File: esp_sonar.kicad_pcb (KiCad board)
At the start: 2 copper layers, 5 parts, among them Q1 2N4401

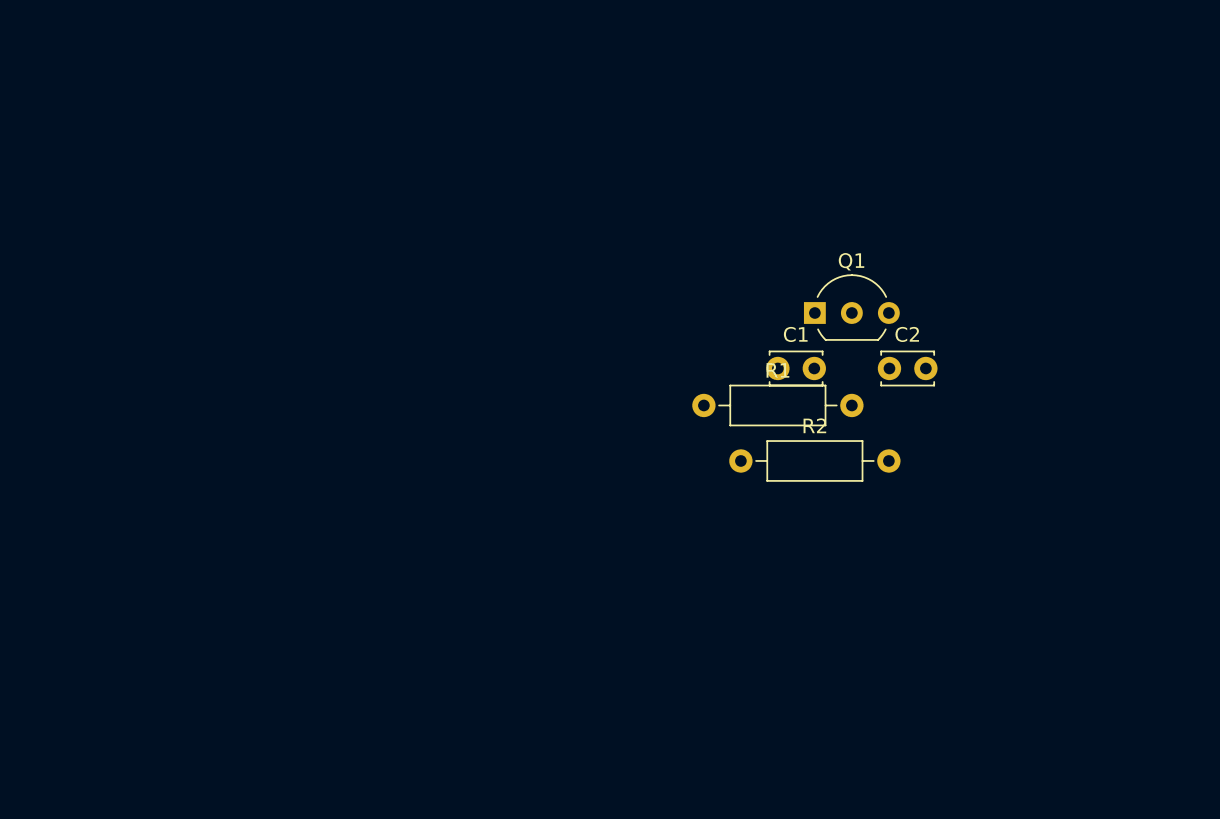
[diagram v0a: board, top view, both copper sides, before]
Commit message: Output driver works, but is overkill
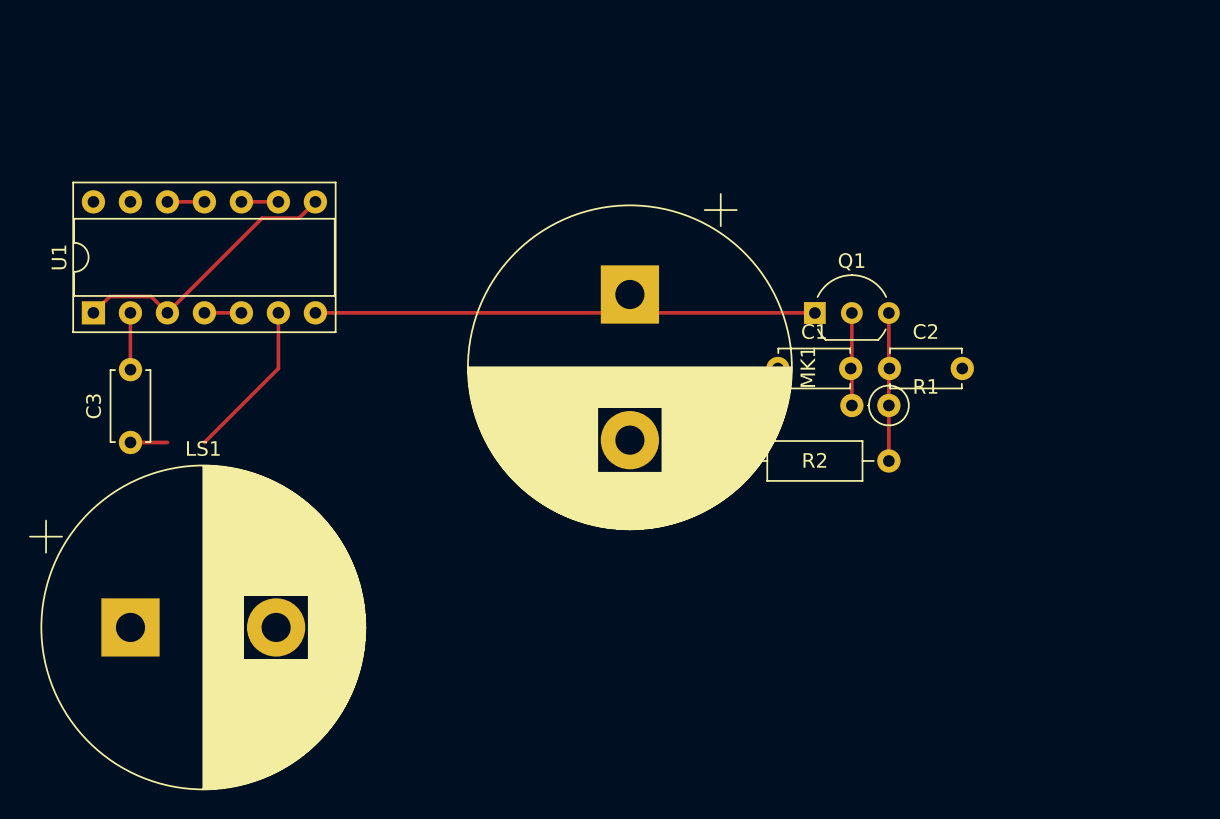
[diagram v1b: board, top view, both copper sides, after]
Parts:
- added C3: 100n, Capacitor_THT:C_Disc_D4.7mm_W2.5mm_P5.00mm, F.Cu at (67.3, 109.2)
- added LS1: Speaker_Ultrasound, Capacitor_THT:CP_Radial_D22.0mm_P10.00mm_SnapIn, F.Cu at (67.3, 121.9)
- added MK1: Microphone_Ultrasound, Capacitor_THT:CP_Radial_D22.0mm_P10.00mm_SnapIn, F.Cu at (101.6, 99.1)
- added U1: 74HC04, Package_DIP:DIP-14_W7.62mm_Socket, F.Cu at (64.8, 100.3)
- C1, C2: footprint Capacitor_THT:C_Disc_D3.4mm_W2.1mm_P2.50mm -> Capacitor_THT:C_Disc_D4.7mm_W2.5mm_P5.00mm
- R1: value 10k -> 100k; footprint Resistor_THT:R_Axial_DIN0207_L6.3mm_D2.5mm_P10.16mm_Horizontal -> Resistor_THT:R_Axial_DIN0207_L6.3mm_D2.5mm_P2.54mm_Vertical
- moved R1 12.7 mm to (119.4, 106.7), turned to 180 degrees
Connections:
- net /Vout renamed /ADC
- C2 pad 1: Net-(C2-Pad1) -> Net-(R1-Pad1)
- Q1 pad 3: Net-(C2-Pad1) -> Net-(R1-Pad1)
- R1 pad 1: +5V -> Net-(R1-Pad1)
- R2 pad 2: Net-(C2-Pad1) -> Net-(R1-Pad1)
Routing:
- net GND: track 0.00 -> 34.3 mm
- net Net-(U1-Pad1): track 0.00 -> 19.3 mm
- net Net-(LS1-Pad2): track 0.00 -> 11.0 mm
- net Net-(R1-Pad1): track 0.00 -> 10.2 mm
- net Net-(C1-Pad2): track 0.00 -> 6.35 mm
- net Net-(C3-Pad2): track 0.00 -> 3.90 mm
- net Net-(U1-Pad11): track 0.00 -> 2.54 mm
- net Net-(U1-Pad10): track 0.00 -> 2.54 mm
- net Net-(U1-Pad5): track 0.00 -> 2.54 mm
- net Net-(C3-Pad1): track 0.00 -> 2.54 mm

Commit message: Protoboard layout
Simplified driver to single-stage mosfet inverter
Keeping the speakers off-board to maintain form factor
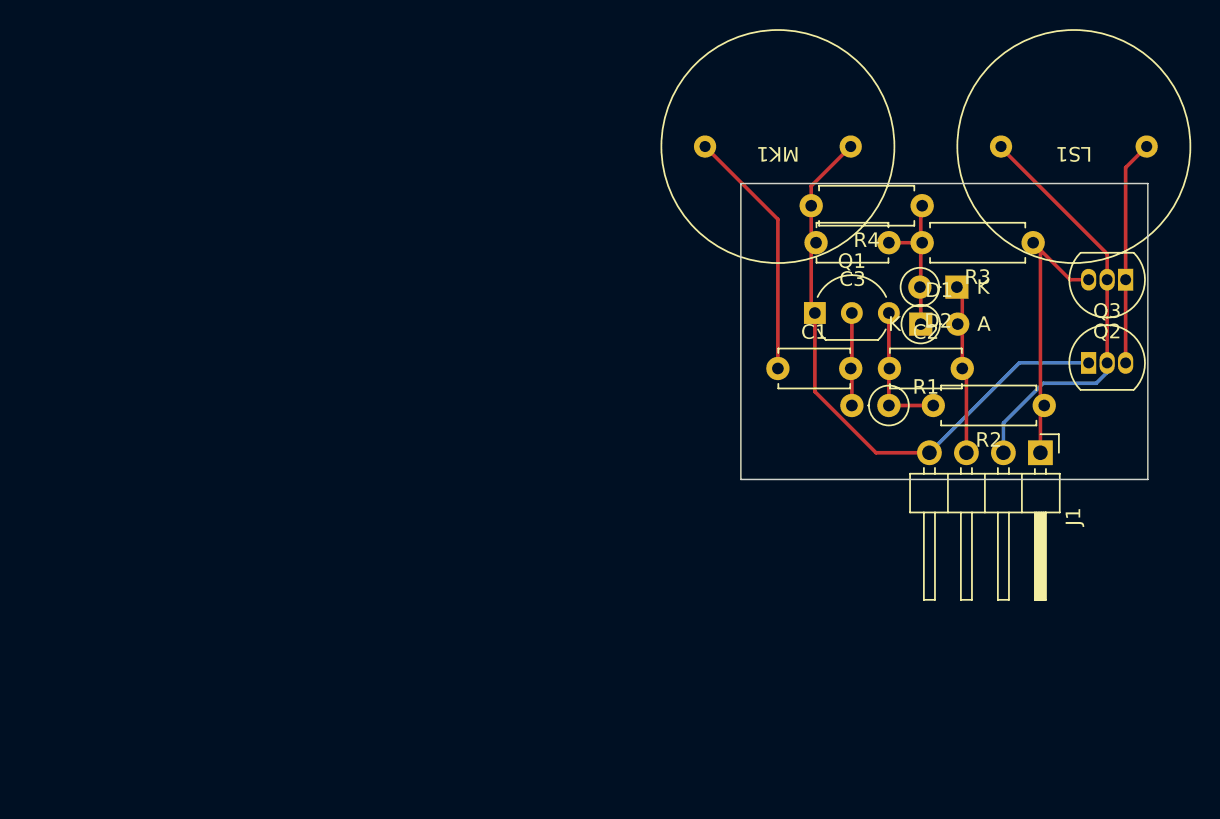
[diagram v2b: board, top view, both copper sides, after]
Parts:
- removed U1: 74HC04, Package_DIP:DIP-14_W7.62mm_Socket
- added D1: 1N4148, Diode_THT:D_DO-35_SOD27_P2.54mm_Vertical_AnodeUp, F.Cu at (121.6, 101.1)
- added D2: 1N4148, Diode_THT:D_DO-35_SOD27_P2.54mm_Vertical_KathodeUp, F.Cu at (124.1, 98.6)
- added J1: Conn_01x04_Male, Connector_PinHeader_2.54mm:PinHeader_1x04_P2.54mm_Horizontal, F.Cu at (129.8, 109.9)
- added Q2: BS250, Package_TO_SOT_THT:TO-92_Inline, F.Cu at (135.6, 98.0)
- added Q3: 2N7000, Package_TO_SOT_THT:TO-92_Inline, F.Cu at (133.1, 103.8)
- added R3: 1M, Resistor_THT:R_Axial_DIN0207_L6.3mm_D2.5mm_P7.62mm_Horizontal, F.Cu at (129.3, 95.5)
- added R4: 100k, Resistor_THT:R_Axial_DIN0207_L6.3mm_D2.5mm_P7.62mm_Horizontal, F.Cu at (121.7, 93.0)
- C3: value 100n -> 10n
- LS1, MK1: footprint Capacitor_THT:CP_Radial_D22.0mm_P10.00mm_SnapIn -> esp_sonar:crystal_speaker
- R2: footprint Resistor_THT:R_Axial_DIN0207_L6.3mm_D2.5mm_P10.16mm_Horizontal -> Resistor_THT:R_Axial_DIN0207_L6.3mm_D2.5mm_P7.62mm_Horizontal
- moved LS1 72.7 mm to (132.1, 88.9), turned to 180 degrees
- moved C3 53.8 mm to (119.4, 95.5), turned to 180 degrees
- moved R2 21.2 mm to (130.0, 106.7), turned to 180 degrees
- moved MK1 14.4 mm to (111.8, 88.9), turned to 180 degrees
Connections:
- C2 pad 2: /ADC -> /RX
- C3 pad 1: Net-(C3-Pad1) -> Net-(D2-Pad2)
- C3 pad 2: Net-(C3-Pad2) -> GND
- LS1 pad 1: Net-(C3-Pad1) -> Net-(LS1-Pad1)
- LS1 pad 2: Net-(LS1-Pad2) -> /TX
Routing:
- net /TX: track 0.00 -> 29.4 mm
- net +5V: track 0.00 -> 19.5 mm
- net Net-(U1-Pad1): track 19.3 -> 0.00 mm
- net /Vin: track 0.00 -> 17.3 mm
- net Net-(LS1-Pad1): track 0.00 -> 15.5 mm
- net /RX: track 0.00 -> 11.6 mm
- net Net-(LS1-Pad2): track 11.0 -> 0.00 mm
- net Net-(D2-Pad2): track 0.00 -> 10.8 mm
- net GND: track 34.3 -> 41.3 mm
- net Net-(C3-Pad2): track 3.90 -> 0.00 mm
- net Net-(U1-Pad11): track 2.54 -> 0.00 mm
- net Net-(U1-Pad10): track 2.54 -> 0.00 mm
- net Net-(U1-Pad5): track 2.54 -> 0.00 mm
- net Net-(C3-Pad1): track 2.54 -> 0.00 mm
- net Net-(C2-Pad1): track 10.2 -> 9.40 mm
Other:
- board outline added: 27.9 x 20.3 mm

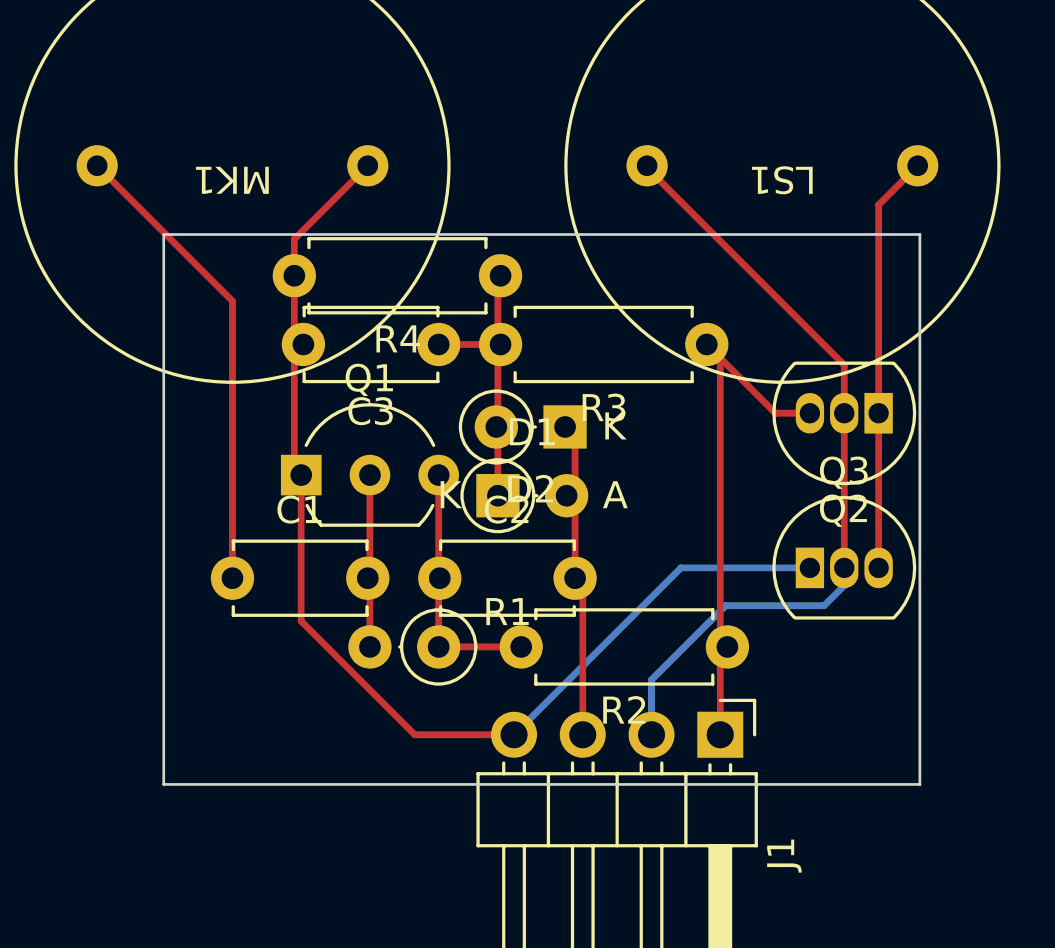
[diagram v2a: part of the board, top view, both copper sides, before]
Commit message: Improved layout
Added R5 to prevent shoot-through when dle
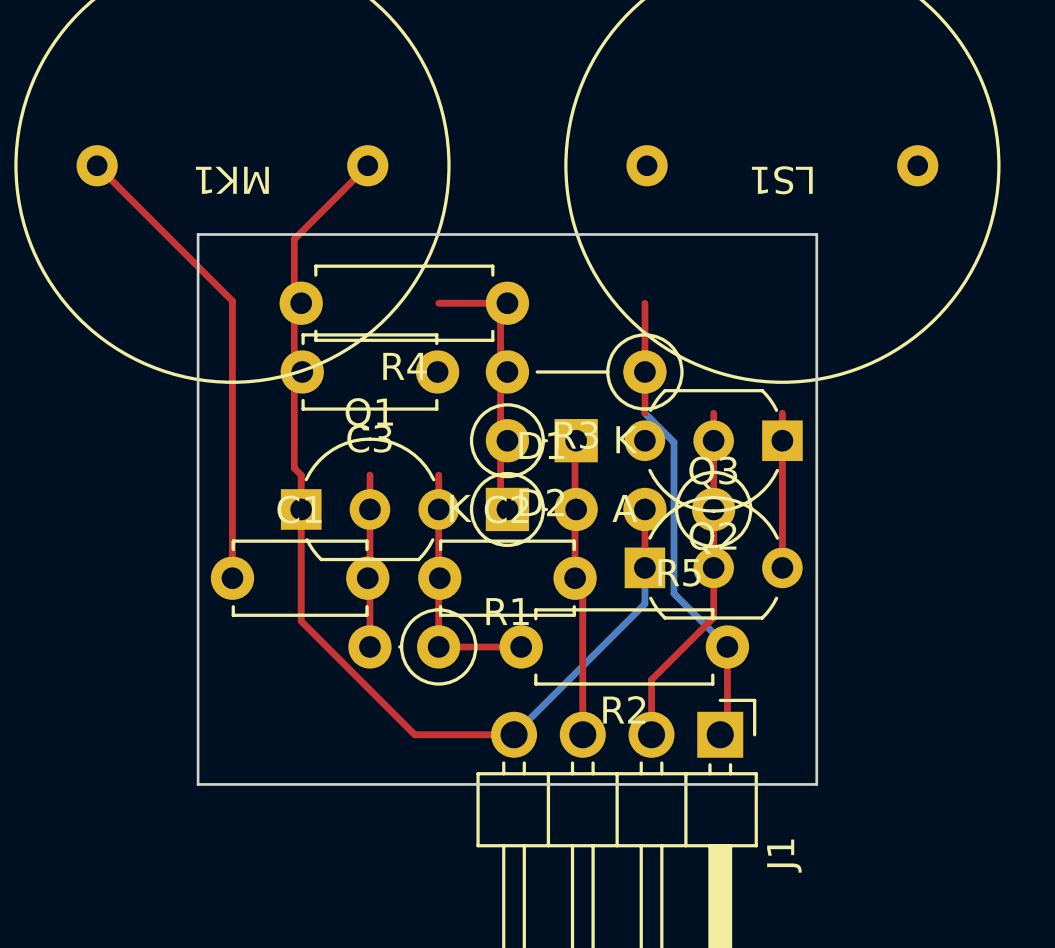
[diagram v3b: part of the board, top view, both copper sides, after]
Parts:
- added R5: 100k, Resistor_THT:R_Axial_DIN0207_L6.3mm_D2.5mm_P2.54mm_Vertical, F.Cu at (129.5, 101.6)
- Q2, Q3: footprint Package_TO_SOT_THT:TO-92_Inline -> Package_TO_SOT_THT:TO-92_Inline_Wide
- R3: footprint Resistor_THT:R_Axial_DIN0207_L6.3mm_D2.5mm_P7.62mm_Horizontal -> Resistor_THT:R_Axial_DIN0207_L6.3mm_D2.5mm_P5.08mm_Vertical
- moved Q3 6.10 mm to (127.0, 103.8)
- moved Q2 3.70 mm to (132.1, 99.1)
- moved R3 2.50 mm to (127.0, 96.5)
- moved Q1 1.27 mm to (114.3, 101.6)
- moved R4 1.05 mm to (121.9, 94.0)
- moved C3 1.02 mm to (119.3, 96.5)
- moved D2 0.65 mm to (124.5, 99.1)
- moved D1 0.62 mm to (121.9, 101.6)
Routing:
- net /TX: track 29.4 -> 12.8 mm
- net Net-(LS1-Pad1): track 15.5 -> 5.72 mm
- net GND: track 41.3 -> 38.0 mm
- net +5V: track 19.5 -> 17.3 mm
- net Net-(D2-Pad2): track 10.8 -> 9.44 mm
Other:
- board size 27.9 x 20.3 mm -> 22.9 x 20.3 mm

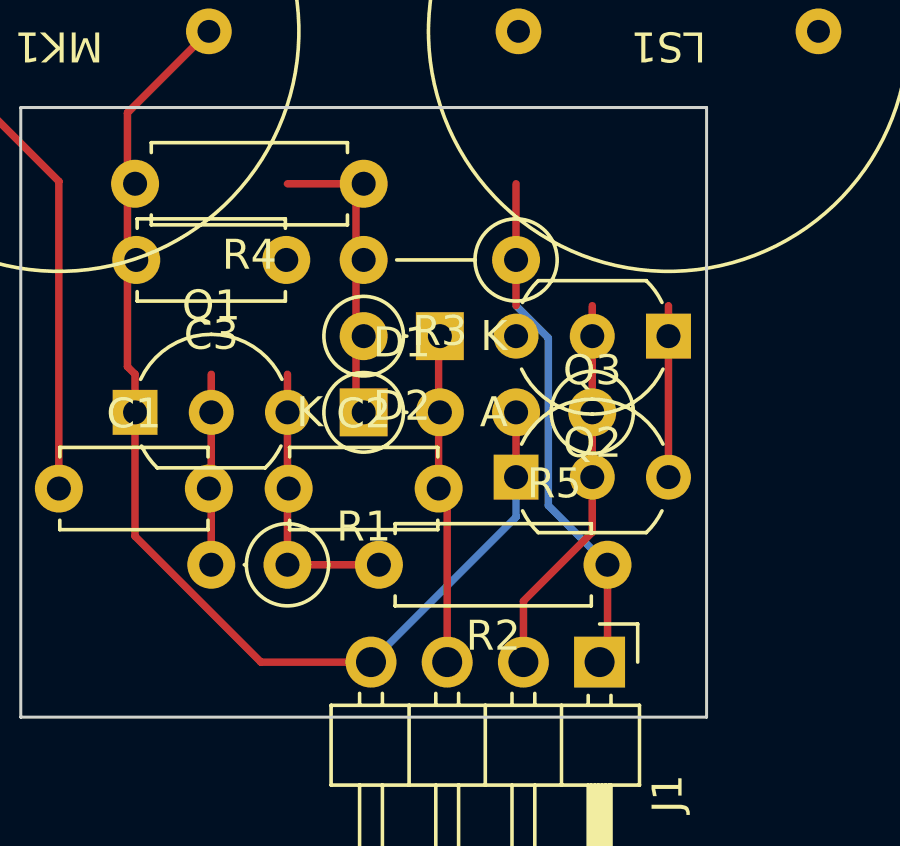
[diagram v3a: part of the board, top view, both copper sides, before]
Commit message: Replaced high-side mosfet with resistor to prevent shoot-through
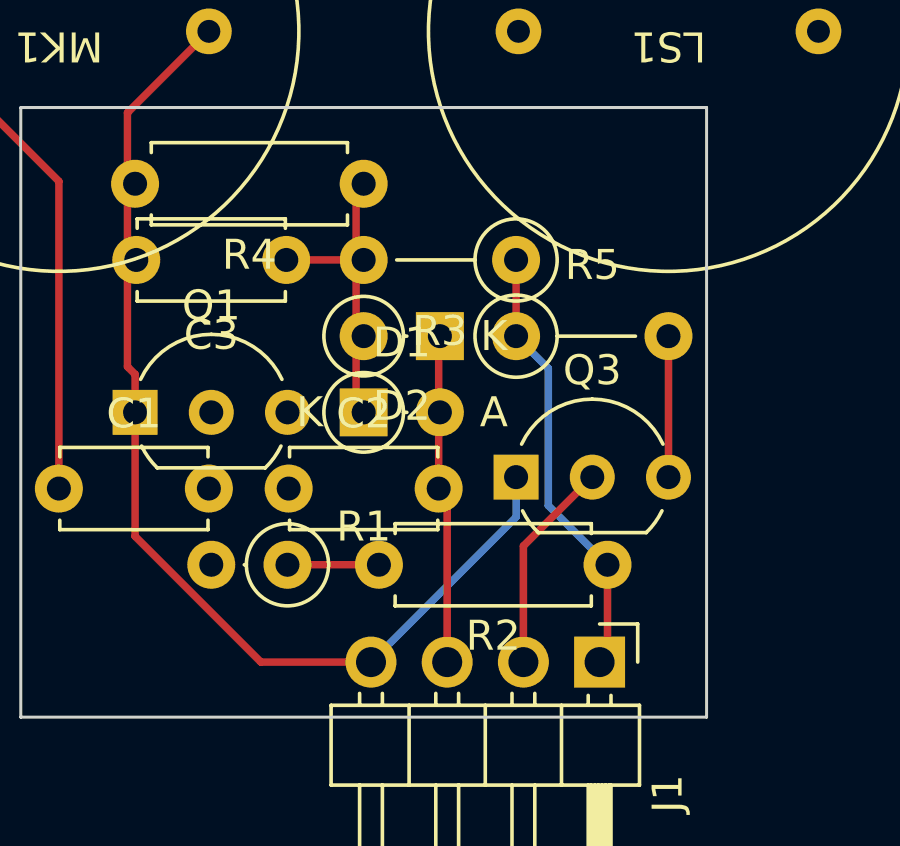
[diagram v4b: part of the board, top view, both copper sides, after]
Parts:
- removed Q2: BS250, Package_TO_SOT_THT:TO-92_Inline_Wide
- R5: value 100k -> 100; footprint Resistor_THT:R_Axial_DIN0207_L6.3mm_D2.5mm_P2.54mm_Vertical -> Resistor_THT:R_Axial_DIN0207_L6.3mm_D2.5mm_P5.08mm_Vertical
- moved R5 3.59 mm to (127.0, 99.1), turned to 0 degrees
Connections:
- R5 pad 1: /TX -> +5V
- R5 pad 2: GND -> Net-(LS1-Pad1)
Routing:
- net Net-(C2-Pad1): track 9.40 -> 3.05 mm
- net Net-(C1-Pad2): track 6.35 -> 0.00 mm
- net /TX: track 12.8 -> 7.12 mm
- net +5V: track 17.3 -> 14.8 mm
- net GND: track 38.0 -> 35.8 mm
- net Net-(LS1-Pad1): track 5.72 -> 4.70 mm
- net /RX: track 11.6 -> 11.1 mm
